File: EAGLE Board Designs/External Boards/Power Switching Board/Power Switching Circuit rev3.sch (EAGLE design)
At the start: 62 parts, among them J1 CONNECTOR-3_, J2 CONNECTOR-4_SOURIAU_, J3 CONNECTOR-4_SOURIAU_, Q1 TRANSISTOR_N_MOS_2-7K1S_TK100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, Q2 TRANSISTOR_N_MOS_2-7K1S_TK100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, Q3 TRANSISTOR_N_MOS_2-7K1S_TK100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, Q4 TRANSISTOR_N_MOS_2-7K1S_TK100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, U1 LTC4421

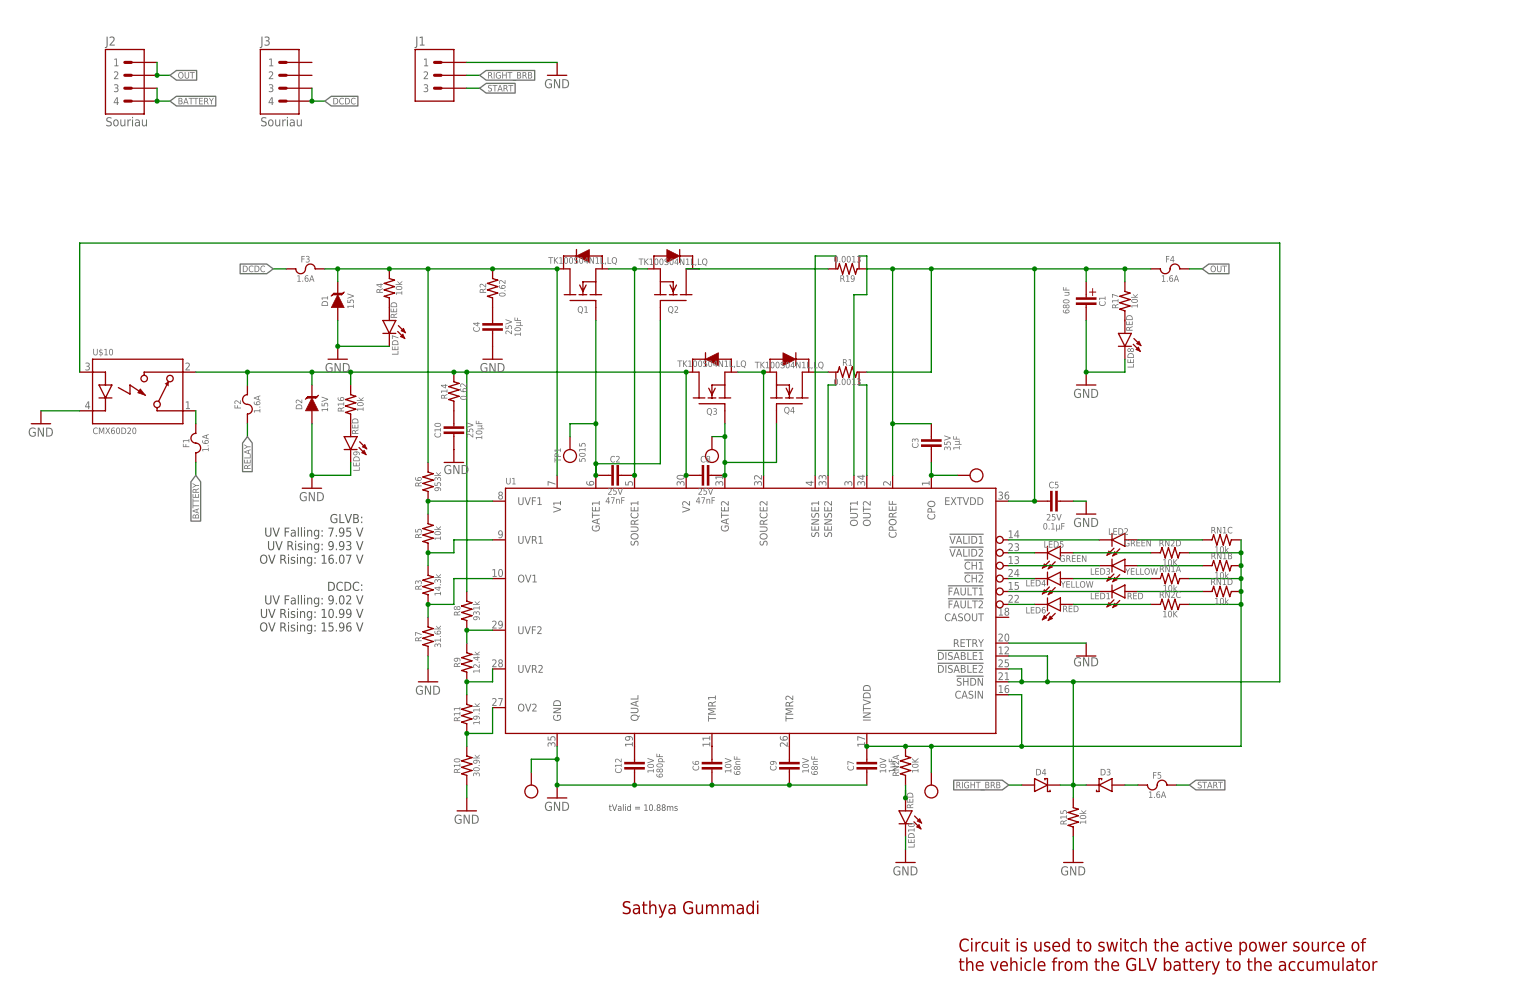
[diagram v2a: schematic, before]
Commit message: Added DCDC converter part
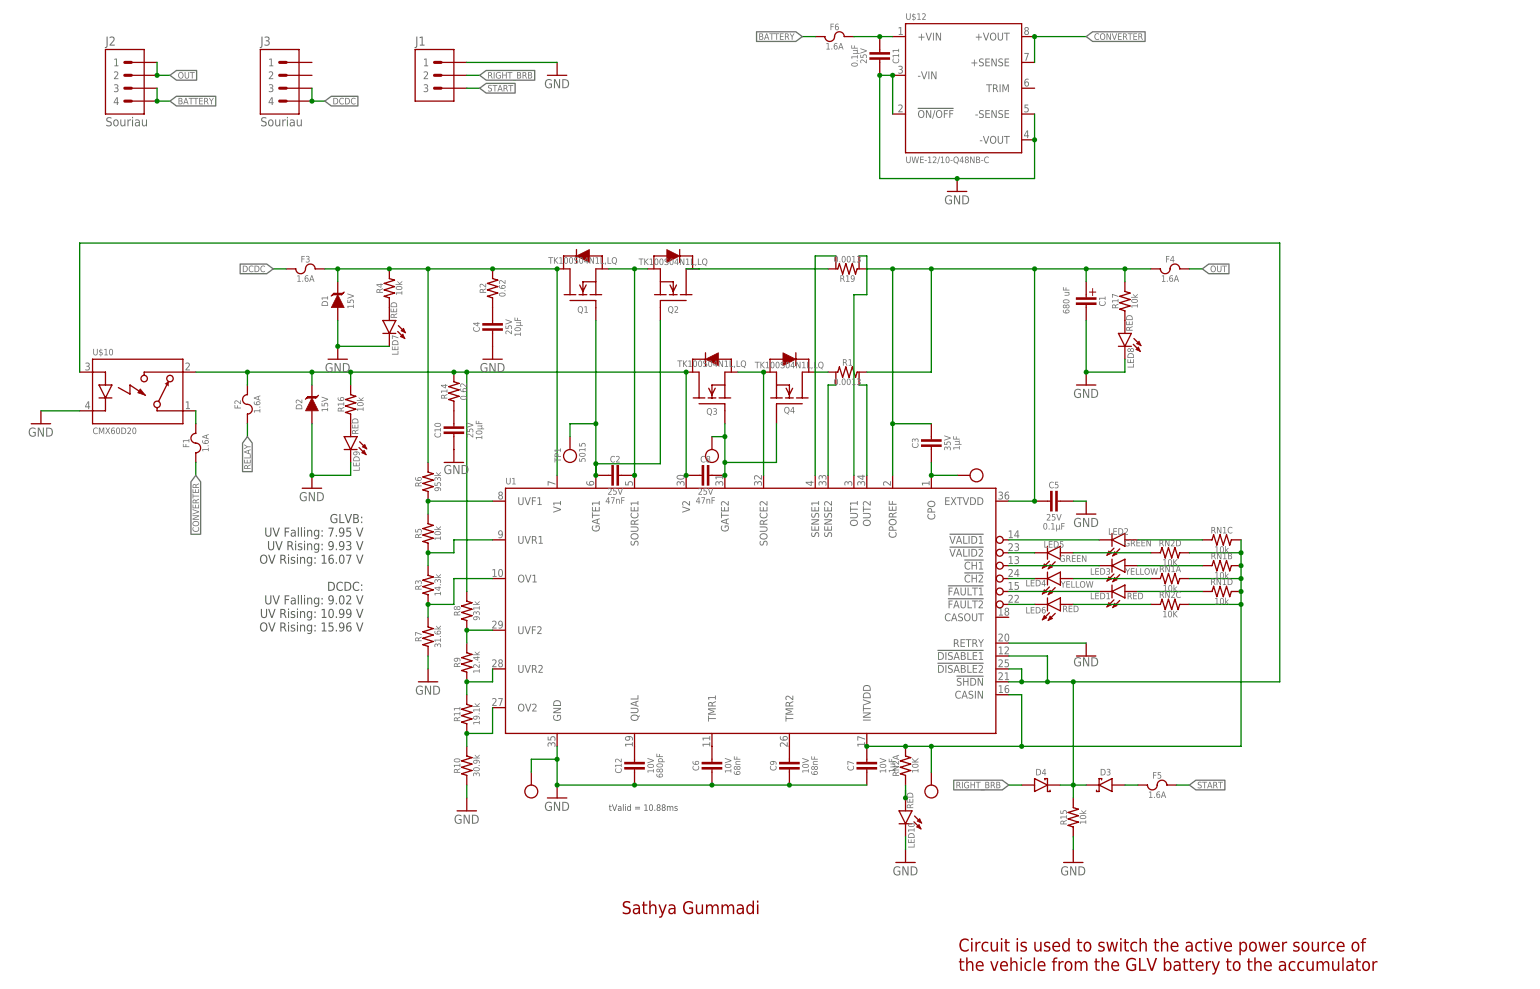
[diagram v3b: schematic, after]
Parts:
- added C11: CAPACITOR_0603_25V_0.1UF, HyTechDevices:CAPACITOR_0603_25V_0.1UF
- added F6: FUSE_0885_1.6, HyTechDevices:FUSE_0885_1.6
- added U$12: UWE-12/10-Q48NB-C, HyTechDevices:UWE-12/10-Q48NB-C
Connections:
- new net CONVERTER: F1.1, U$12.+SENSE, U$12.+VOUT
- new net N$29: C11.2, F6.2, U$12.+VIN
- net BATTERY: now also F6.1; no longer F1.1
- net GND: now also C11.1, U$12.!ON/OFF, U$12.-SENSE, U$12.-VIN, U$12.-VOUT
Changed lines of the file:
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@@
 <part name="TP1" library="HyTechDevices" deviceset="TEST_POINT" device=""/>
 <part name="U$10" library="HyTechDevices" deviceset="RELAY_SOLIDSTATE_NO_?*" device="" technology="CMX60D20"/>
+<part name="U$12" library="HyTechDevices" deviceset="UWE-*" device="" technology="12/10-Q48NB-C"/>
+<part name="F6" library="HyTechDevices" deviceset="FUSE_?_*" device="0885" technology="1.6"/>
+<part name="GND15" library="HyTechSupplies" deviceset="GND" device=""/>
+<part name="C11" library="HyTechDevices" deviceset="CAPACITOR_?_*" device="0603" technology="25V_0.1UF"/>
 </parts>
 <sheets>
@@
 <attribute name="MPN" x="-111.76" y="14.478" size="1.27" layer="96" align="top-left"/>
 </instance>
+<instance part="U$12" gate="G$1" x="48.26" y="93.98" smashed="yes">
+<attribute name="NAME" x="48.26" y="94.742" size="1.27" layer="95"/>
+<attribute name="MPN" x="48.26" y="67.818" size="1.27" layer="95" align="top-left"/>
+</instance>
+<instance part="F6" gate="G$1" x="35.56" y="91.44" smashed="yes">
+<attribute name="NAME" x="34.29" y="92.71" size="1.27" layer="95" align="bottom-center"/>
+<attribute name="CURRENT" x="34.29" y="90.17" size="1.27" layer="96" align="top-center"/>
+</instance>
+<instance part="GND15" gate="1" x="58.42" y="60.96" smashed="yes">
+<attribute name="VALUE" x="55.88" y="58.42" size="1.778" layer="96"/>
+</instance>
+<instance part="C11" gate="G$1" x="43.18" y="86.36" smashed="yes" rot="R270">
+<attribute name="NAME" x="45.72" y="87.63" size="1.27" layer="95" rot="R270" align="bottom-center"/>
+<attribute name="VOLTAGE" x="40.64" y="87.63" size="1.27" layer="96" rot="R270" align="top-center"/>
+<attribute name="CAPACITANCE" x="38.862" y="87.63" size="1.27" layer="96" rot="R270" align="top-center"/>
+</instance>
 </instances>
 <busses>
@@
 <wire x1="-114.3" y1="17.78" x2="-121.92" y2="17.78" width="0.1524" layer="91"/>
 </segment>
+<segment>
+<pinref part="U$12" gate="G$1" pin="-VIN"/>
+<pinref part="U$12" gate="G$1" pin="!ON/OFF"/>
+<wire x1="45.72" y1="76.2" x2="45.72" y2="83.82" width="0.1524" layer="91"/>
+<junction x="45.72" y="83.82"/>
+<wire x1="45.72" y1="83.82" x2="43.18" y2="83.82" width="0.1524" layer="91"/>
+<pinref part="C11" gate="G$1" pin="1"/>
+<pinref part="GND15" gate="1" pin="GND"/>
+<wire x1="43.18" y1="83.82" x2="43.18" y2="63.5" width="0.1524" layer="91"/>
+<wire x1="43.18" y1="63.5" x2="58.42" y2="63.5" width="0.1524" layer="91"/>
+<junction x="43.18" y="83.82"/>
+<pinref part="U$12" gate="G$1" pin="-VOUT"/>
+<pinref part="U$12" gate="G$1" pin="-SENSE"/>
+<wire x1="73.66" y1="71.12" x2="73.66" y2="76.2" width="0.1524" layer="91"/>
+<wire x1="58.42" y1="63.5" x2="73.66" y2="63.5" width="0.1524" layer="91"/>
+<wire x1="73.66" y1="63.5" x2="73.66" y2="71.12" width="0.1524" layer="91"/>
+<junction x="58.42" y="63.5"/>
+<junction x="73.66" y="71.12"/>
+</segment>
 </net>
 <net name="BATTERY" class="0">
@@
 </segment>
 <segment>
-<pinref part="F1" gate="G$1" pin="1"/>
-<wire x1="-91.44" y1="7.62" x2="-91.44" y2="5.08" width="0.1524" layer="91"/>
-<label x="-91.44" y="5.08" size="1.27" layer="95" rot="R270" xref="yes"/>
+<pinref part="F6" gate="G$1" pin="1"/>
+<wire x1="30.48" y1="91.44" x2="27.94" y2="91.44" width="0.1524" layer="91"/>
+<label x="27.94" y="91.44" size="1.27" layer="95" rot="R180" xref="yes"/>
 </segment>
 </net>
@@
 </segment>
 </net>
+<net name="N$29" class="0">
+<segment>
+<pinref part="U$12" gate="G$1" pin="+VIN"/>
+<wire x1="45.72" y1="91.44" x2="43.18" y2="91.44" width="0.1524" layer="91"/>
+<pinref part="F6" gate="G$1" pin="2"/>
+<pinref part="C11" gate="G$1" pin="2"/>
+<wire x1="43.18" y1="91.44" x2="38.1" y2="91.44" width="0.1524" layer="91"/>
+<junction x="43.18" y="91.44"/>
+</segment>
+</net>
+<net name="CONVERTER" class="0">
+<segment>
+<pinref part="U$12" gate="G$1" pin="+VOUT"/>
+<wire x1="73.66" y1="91.44" x2="83.82" y2="91.44" width="0.1524" layer="91"/>
+<label x="83.82" y="91.44" size="1.27" layer="95" xref="yes"/>
+<pinref part="U$12" gate="G$1" pin="+SENSE"/>
+<wire x1="73.66" y1="86.36" x2="73.66" y2="91.44" width="0.1524" layer="91"/>
+<junction x="73.66" y="91.44"/>
+</segment>
+<segment>
+<pinref part="F1" gate="G$1" pin="1"/>
+<wire x1="-91.44" y1="7.62" x2="-91.44" y2="5.08" width="0.1524" layer="91"/>
+<label x="-91.44" y="5.08" size="1.27" layer="95" rot="R270" xref="yes"/>
+</segment>
+</net>

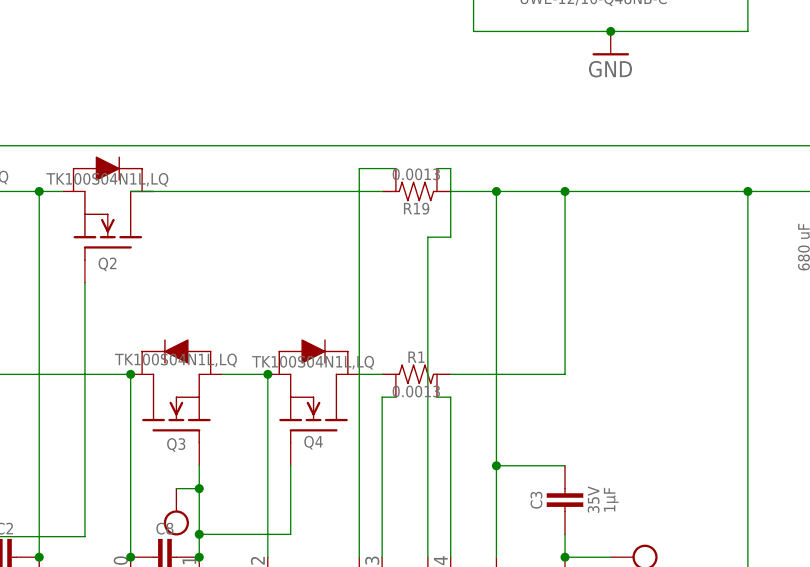
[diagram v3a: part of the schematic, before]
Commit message: Replaced sense resistors with ones in library
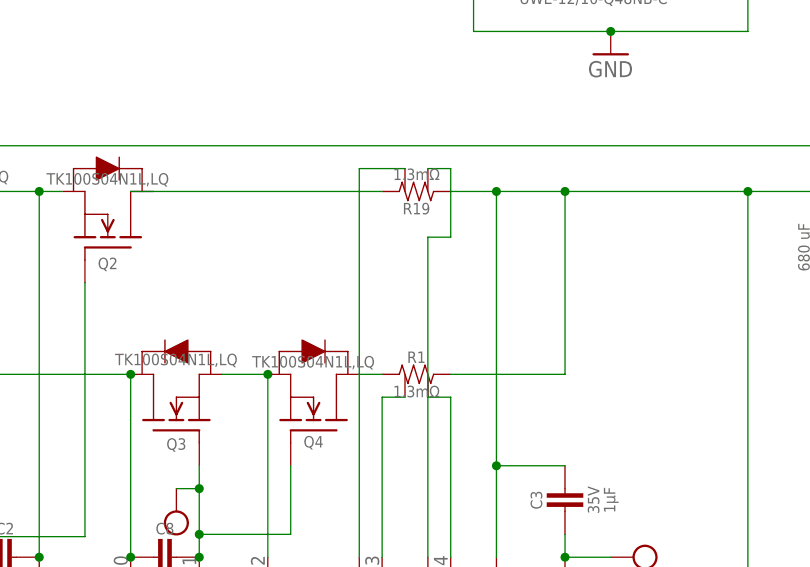
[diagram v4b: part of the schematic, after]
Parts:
- R1, R19: value RESISTOR_SENSE -> RESISTOR_SENSE_0.0013; device HyTechDevices:RESISTOR_SENSE -> HyTechDevices:RESISTOR_SENSE_0.0013
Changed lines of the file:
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@@
 <part name="J1" library="HyTechDevices" deviceset="CONNECTOR-3_?" device=""/>
 <part name="GND7" library="HyTechSymbols" deviceset="GND" device=""/>
-<part name="R1" library="HyTechDevices" deviceset="RESISTOR_SENSE" device=""/>
+<part name="R1" library="HyTechDevices" deviceset="RESISTOR_SENSE_*" device="" technology="0.0013"/>
 <part name="C1" library="HyTechDevices" deviceset="CAPACITOR_POLARIZED" device=""/>
 <part name="U$7" library="HyTechDevices" deviceset="TEST_POINT" device=""/>
@@
 <part name="LED8" library="HyTechDevices" deviceset="LED_?_*" device="0603" technology="RED" value="RED"/>
 <part name="R17" library="HyTechDevices" deviceset="RESISTOR" device="0603" value="10k"/>
-<part name="R19" library="HyTechDevices" deviceset="RESISTOR_SENSE" device=""/>
+<part name="R19" library="HyTechDevices" deviceset="RESISTOR_SENSE_*" device="" technology="0.0013"/>
 <part name="Q1" library="HyTechDevices" deviceset="TRANSISTOR_N_MOS_?_*" device="2-7K1S" technology="TK100S04N1L,LQ"/>
 <part name="Q2" library="HyTechDevices" deviceset="TRANSISTOR_N_MOS_?_*" device="2-7K1S" technology="TK100S04N1L,LQ"/>
@@
 <wire x1="30.48" y1="5.08" x2="30.48" y2="48.26" width="0.1524" layer="91"/>
 <pinref part="R19" gate="G$1" pin="4"/>
-<wire x1="34.544" y1="48.26" x2="30.48" y2="48.26" width="0.1524" layer="91"/>
+<wire x1="35.56" y1="48.26" x2="30.48" y2="48.26" width="0.1524" layer="91"/>
 </segment>
 </net>
@@
 <wire x1="33.02" y1="5.08" x2="33.02" y2="22.86" width="0.1524" layer="91"/>
 <pinref part="R1" gate="G$1" pin="3"/>
-<wire x1="33.02" y1="22.86" x2="34.544" y2="22.86" width="0.1524" layer="91"/>
+<wire x1="33.02" y1="22.86" x2="35.56" y2="22.86" width="0.1524" layer="91"/>
 </segment>
 </net>
@@
 <wire x1="40.64" y1="5.08" x2="40.64" y2="22.86" width="0.1524" layer="91"/>
 <pinref part="R1" gate="G$1" pin="4"/>
-<wire x1="40.64" y1="22.86" x2="39.116" y2="22.86" width="0.1524" layer="91"/>
+<wire x1="40.64" y1="22.86" x2="38.1" y2="22.86" width="0.1524" layer="91"/>
 </segment>
 </net>
@@
 <wire x1="40.64" y1="40.64" x2="40.64" y2="48.26" width="0.1524" layer="91"/>
 <pinref part="R19" gate="G$1" pin="3"/>
-<wire x1="40.64" y1="48.26" x2="39.116" y2="48.26" width="0.1524" layer="91"/>
-</segment>
-</net>
+<wire x1="40.64" y1="48.26" x2="38.1" y2="48.26" width="0.1524" layer="91"/>
+</segment>
+</net>
